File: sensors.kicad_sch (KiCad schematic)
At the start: 0 parts

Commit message: Added some sensors and ch340
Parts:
- added C5: CC0603KRX7R9BB104, easyeda2kicad:C0603, symbol easyeda2kicad:CC0603KRX7R9BB104
- added R11, R12: 0603WAF1002T5E, easyeda2kicad:R0603, symbol easyeda2kicad:0603WAF1002T5E
- added U4: OPT3004DNPR, easyeda2kicad:WSON-6_L2.0-W2.0-P0.65-TL-EP, symbol easyeda2kicad:OPT3004DNPR
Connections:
- new net +3V3: C5.2, R11.2, R12.2, U4.1 (VDD)
- new net GND: C5.1, U4.2 (ADDR), U4.3 (GND), U4.7 (EP)
- new net INT_L: U4.5 (INT)
- new net SCL: R11.1, U4.6 (SDA)
- new net SDA: R12.1, U4.4 (SCL)
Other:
- note added: "i2c address : 0x44"

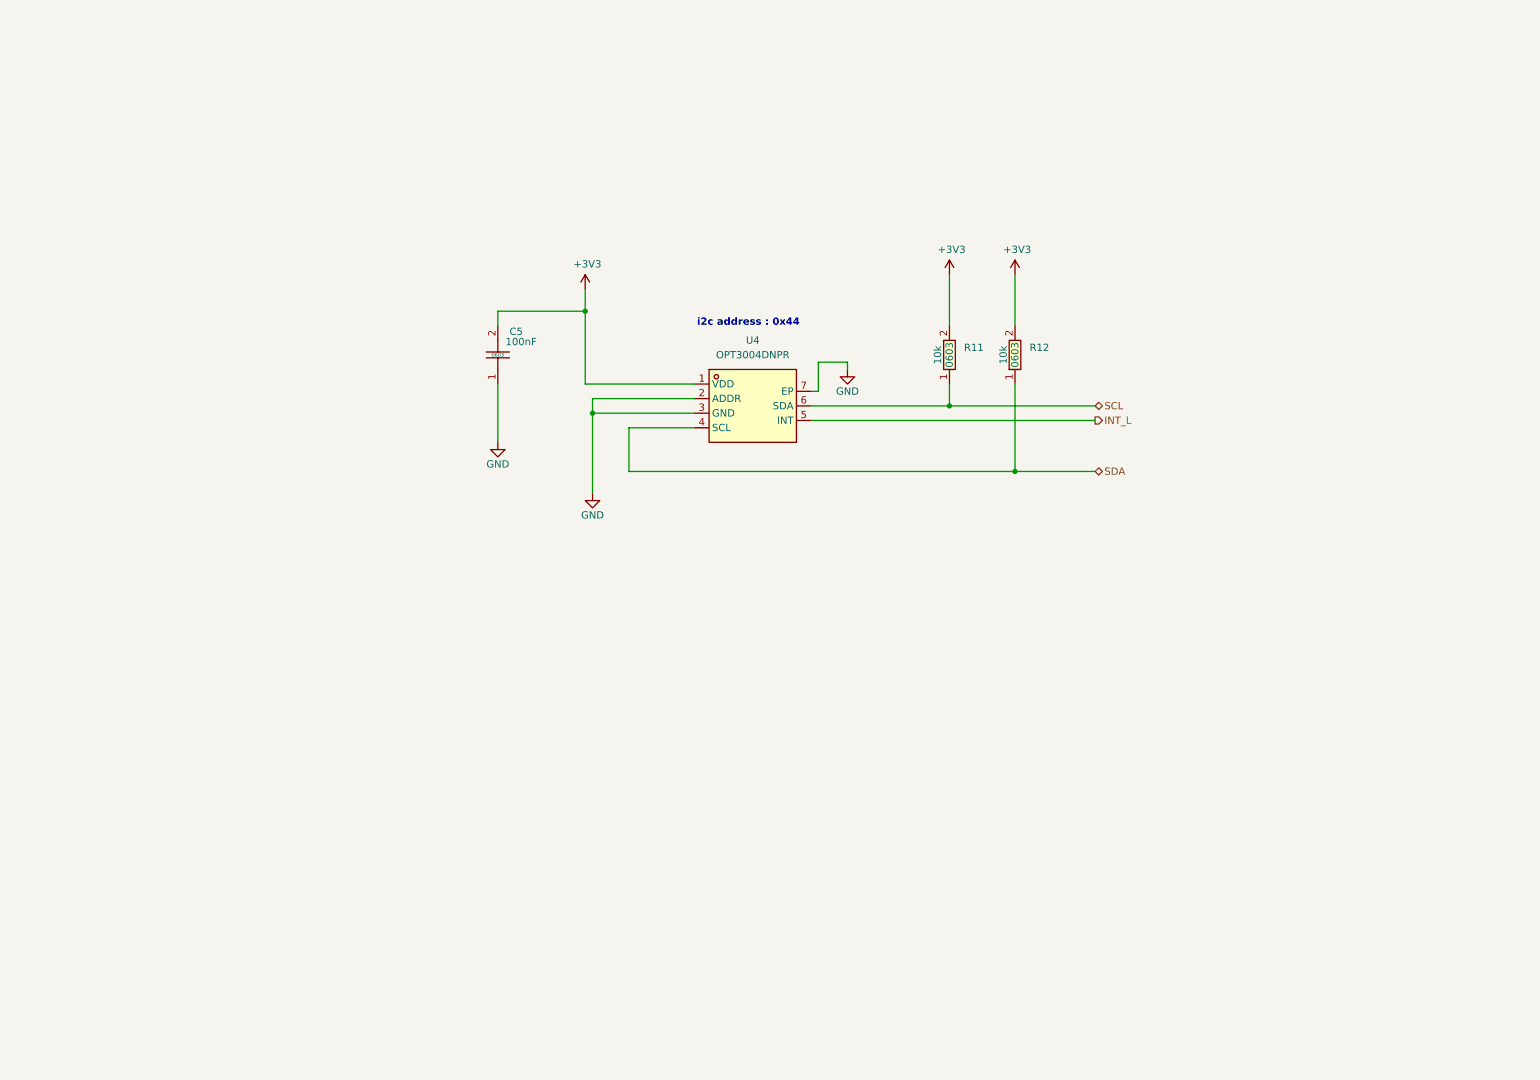
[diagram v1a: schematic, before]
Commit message: Added some sensors and current sensor
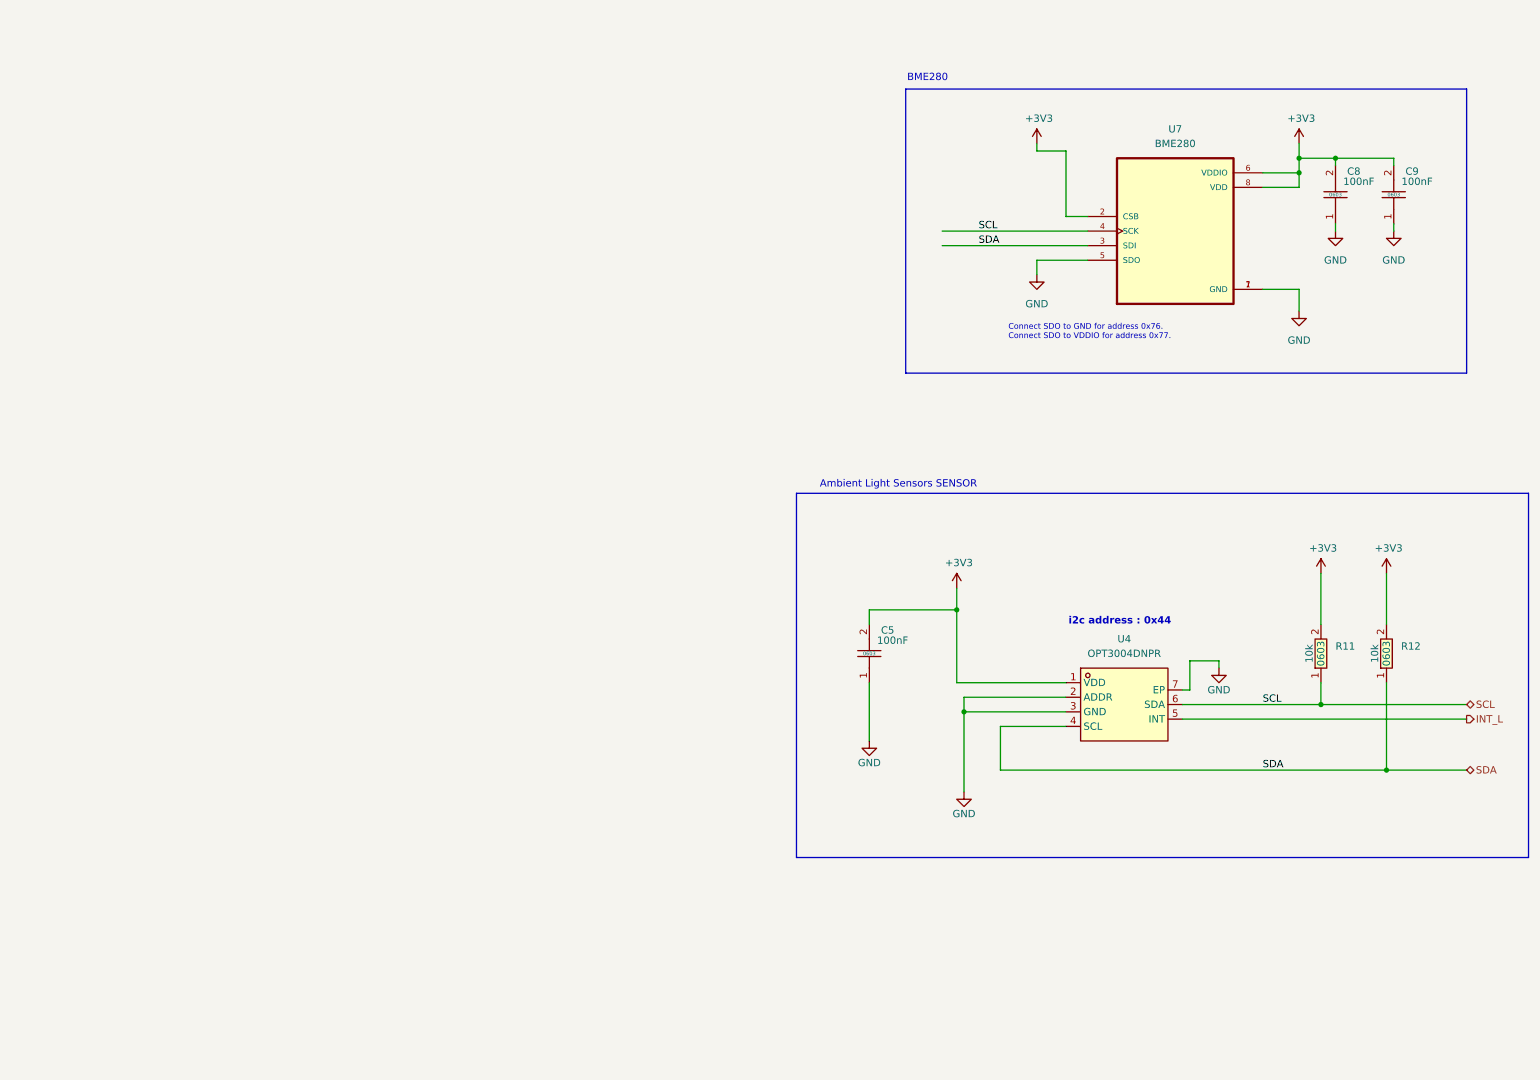
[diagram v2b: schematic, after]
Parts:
- added C8, C9: CC0603KRX7R9BB104, easyeda2kicad:C0603, symbol easyeda2kicad:CC0603KRX7R9BB104
- added U7: BME280, Footprints:PSON65P250X250X100-8N, symbol BME280:BME280
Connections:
- net +3V3: now also C8.2, C9.2, U7.2 (CSB), U7.6 (VDDIO), U7.8 (VDD)
- net GND: now also C8.1, C9.1, U7.1 (GND), U7.5 (SDO), U7.7 (GND)
- net SCL: now also U7.4 (SCK)
- net SDA: now also U7.3 (SDI)
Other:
- note added: "Ambient Light Sensors SENSOR"
- note added: "BME280"
- moved on the sheet: C5, R11, R12, U4

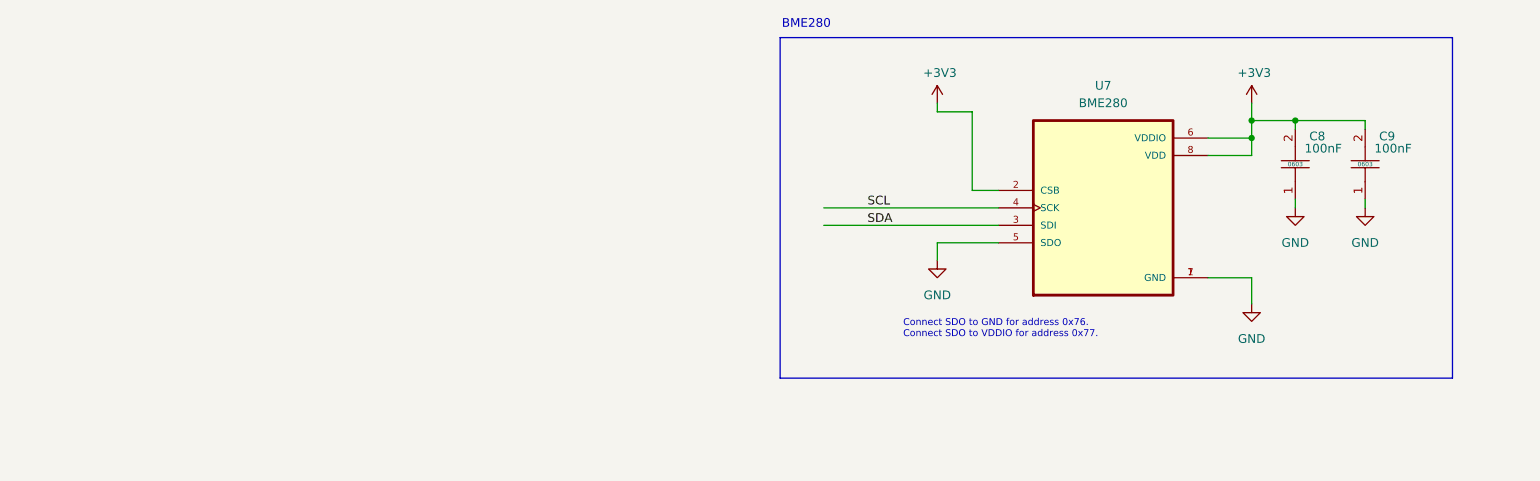
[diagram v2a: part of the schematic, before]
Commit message: Added led matrix and ina260
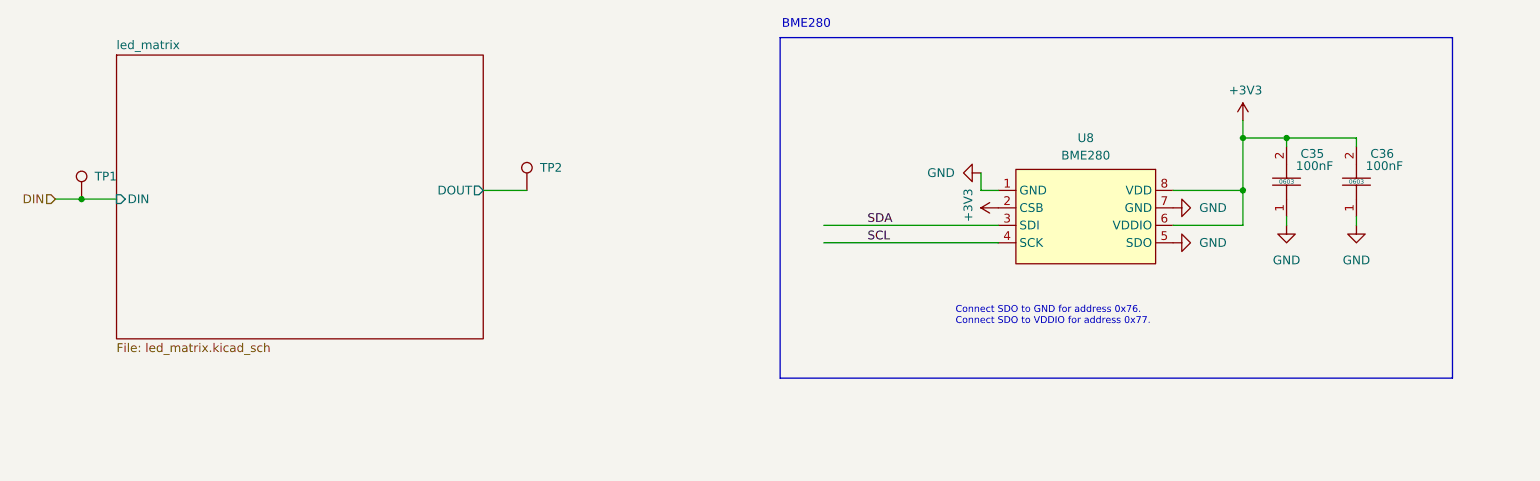
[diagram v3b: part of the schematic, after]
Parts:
- removed C8, C9: CC0603KRX7R9BB104, easyeda2kicad:C0603, symbol easyeda2kicad:CC0603KRX7R9BB104
- removed U7: BME280, Footprints:PSON65P250X250X100-8N, symbol BME280:BME280
- added C35, C36: CC0603KRX7R9BB104, easyeda2kicad:C0603, symbol easyeda2kicad:CC0603KRX7R9BB104
- added TP1, TP2: TestPoint, TestPoint:TestPoint_Pad_2.0x2.0mm, symbol Connector:TestPoint
- added U8: BME280, easyeda2kicad:LGA-8_BME280_BL, symbol easyeda2kicad:BME280
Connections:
- net +3V3: now also C35.2, C36.2, U8.2 (CSB), U8.6 (VDDIO), U8.8 (VDD)
- net GND: now also C35.1, C36.1, U8.1 (GND), U8.5 (SDO), U8.7 (GND)
- net SCL: now also U8.4 (SCK)
- net SDA: now also U8.3 (SDI)
- new net DIN: TP1.1
- new net led_matrix/DOUT: TP2.1
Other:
- added sheet led_matrix (led_matrix.kicad_sch)

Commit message: Finished sensor / usb block
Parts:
- added C37, C8, C9: CC0603KRX7R9BB104, easyeda2kicad:C0603, symbol easyeda2kicad:CC0603KRX7R9BB104
- added Card1: TF PUSH, easyeda2kicad:TF-SMD_TF-PUSH, symbol easyeda2kicad:TFPUSH
- added R18, R19: 0603WAF1002T5E, easyeda2kicad:R0603, symbol easyeda2kicad:0603WAF1002T5E
- added U7: ICM-42688-P, easyeda2kicad:LGA-14_L3.0-W2.5-P0.50-TL, symbol easyeda2kicad:ICM-42688-P
- added U9: SN74AHCT1G125DBVR, easyeda2kicad:SOT-23-5_L3.0-W1.7-P0.95-LS2.8-BR, symbol easyeda2kicad:SN74AHCT1G125DBVR
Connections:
- net +3V3: now also C8.2, C9.2, Card1.4 (VDD), R18.2, R19.2, U7.12 (AP_CS), U7.5 (VDDIO), U7.8 (VDD)
- net DIN: now also U9.2 (A); no longer TP1.1
- net GND: now also C37.1, C8.1, C9.1, Card1.6 (VSS), U7.1 (AP_SDO/AP_AD0), U7.10 (RESV), U7.11 (RESV), U7.2 (RESV), U7.3 (RESV), U7.6 (GND), U7.7 (RESV), U7.9 (INT2/FSYNC/CLKIN), U9.1 (~{OE}), U9.3 (GND)
- net SCL: now also U7.13 (AP_SCL/AP_SCLK)
- net SDA: now also U7.14 (AP_SDA/AP_SDIO/AP_SDI)
- new net +5V: C37.2, U9.5 (VCC)
- new net CD: Card1.9 (CD), R18.1
- new net IMU_INT: U7.4 (INT1/INT)
- new net SPI_CLK: Card1.5 (CLX)
- new net SPI_CS: Card1.2 (CD/DAT3), R19.1
- new net SPI_MISO: Card1.7 (DAT0)
- new net SPI_MOSI: Card1.3 (CMD)
- new net led_matrix/DIN: TP1.1, U9.4 (Y)
- no-connect marks 0 -> 6
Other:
- note added: "IMU 6-AXIS I2C ADDRESS : 0x34"
- note added: "Micro sd card"
- note added: "Temperature , Humidity ,Pressure - Sensor"
- note added: "i2c address : 0x76"
- note removed: "BME280"
- moved on the sheet: TP1, TP2

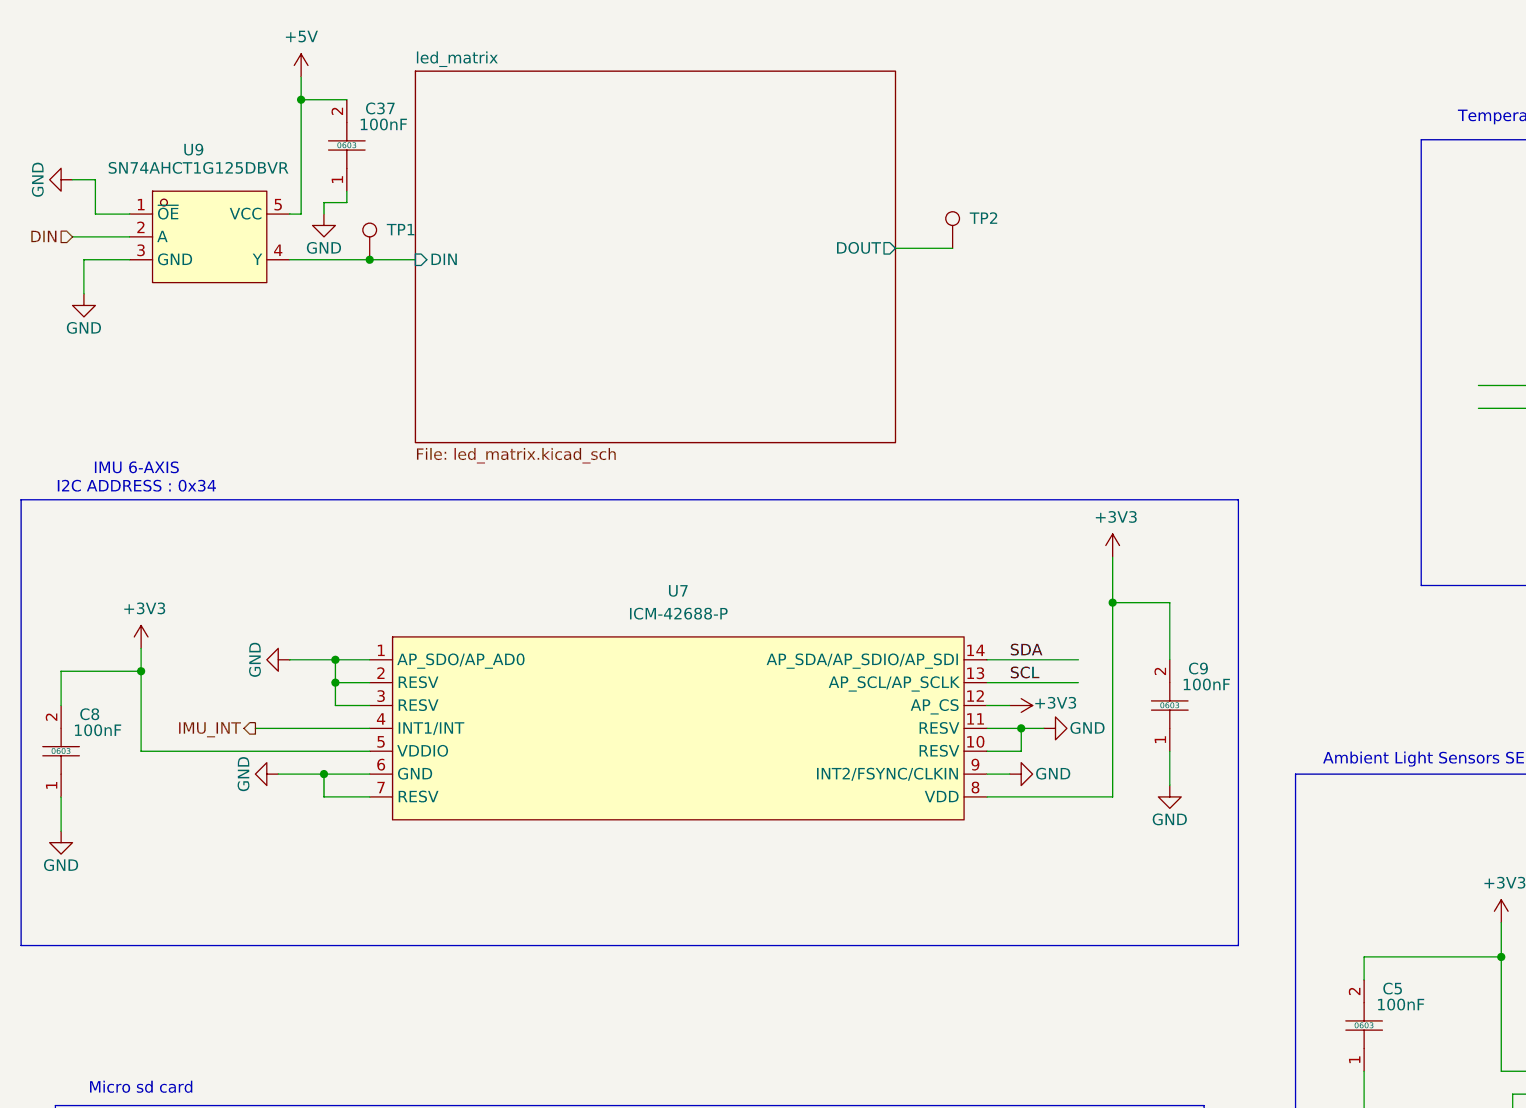
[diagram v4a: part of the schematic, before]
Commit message: Finished schematic need to check , before layout
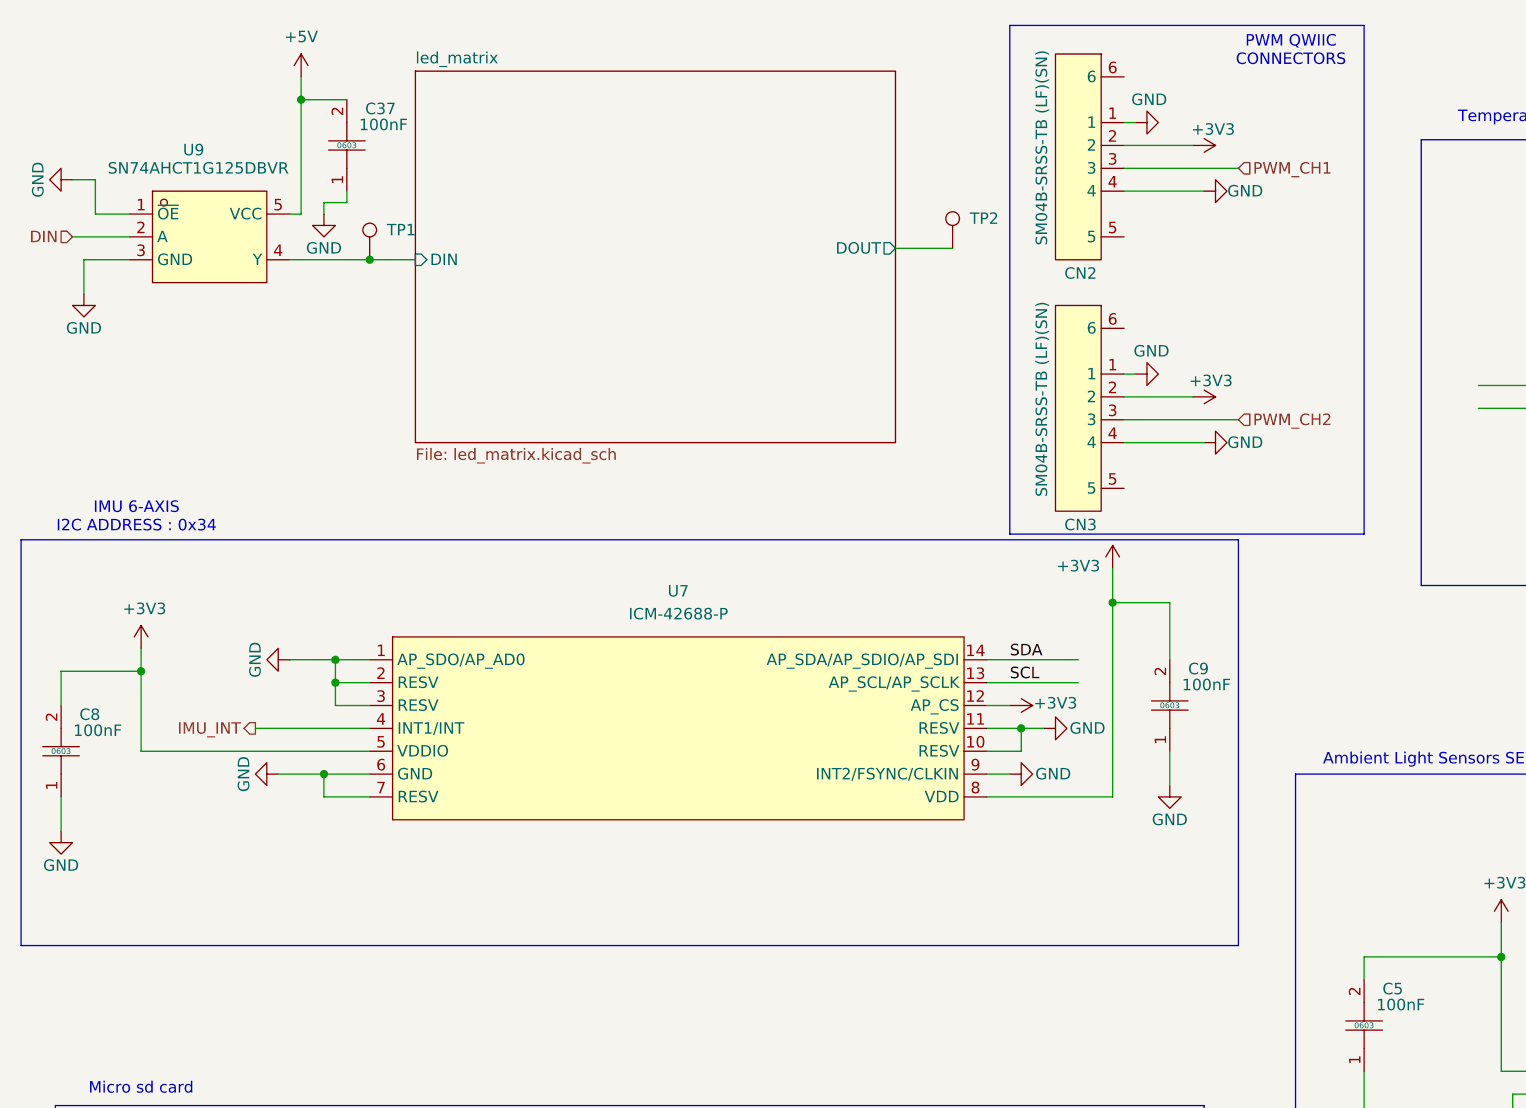
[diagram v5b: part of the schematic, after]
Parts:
- added CN2, CN3: SM04B-SRSS-TB (LF)(SN), easyeda2kicad:CONN-SMD_4P-P1.00_SM04B-SRSS-TB-LF-SN, symbol easyeda2kicad:SM04B-SRSS-TB(LF)(SN)
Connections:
- net +3V3: now also CN2.2, CN3.2
- net GND: now also CN2.1, CN2.4, CN3.1, CN3.4
- new net PWM_CH1: CN2.3
- new net PWM_CH2: CN3.3
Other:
- note added: "PWM QWIIC CONNECTORS"
